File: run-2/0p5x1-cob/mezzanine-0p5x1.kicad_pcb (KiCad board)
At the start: 2 copper layers, 14 x 16 mm, 11 parts

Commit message: Layers, text
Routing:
- added copper zone on In1.Cu, net GND
- added copper zone on In2.Cu, net GND
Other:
- copper layers 2 -> 4
- board text added: "wafer.space GF180MCU Run 2"
- board text removed: "wafer.space GF180MCU Run 1"
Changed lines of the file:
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@@
 	(generator_version "10.0")
 	(general
-		(thickness 1.6)
+		(thickness 0.747)
 		(legacy_teardrops no)
 	)
@@
 	(layers
 		(0 "F.Cu" signal)
+		(4 "In1.Cu" signal)
+		(6 "In2.Cu" signal)
 		(2 "B.Cu" signal)
 		(9 "F.Adhes" user "F.Adhesive")
@@
 			(layer "F.Cu"
 				(type "copper")
-				(thickness 0.035)
+				(thickness 0.0175)
 			)
 			(layer "dielectric 1"
+				(type "prepreg")
+				(thickness 0.196)
+				(material "FR4")
+				(epsilon_r 4.5)
+				(loss_tangent 0.02)
+			)
+			(layer "In1.Cu"
+				(type "copper")
+				(thickness 0.035)
+			)
+			(layer "dielectric 2"
 				(type "core")
-				(thickness 1.51)
+				(thickness 0.23)
 				(material "FR4")
 				(epsilon_r 4.5)
 				(loss_tangent 0.02)
 			)
-			(layer "B.Cu"
+			(layer "In2.Cu"
 				(type "copper")
 				(thickness 0.035)
 			)
+			(layer "dielectric 3"
+				(type "prepreg")
+				(thickness 0.196)
+				(material "FR4")
+				(epsilon_r 4.5)
+				(loss_tangent 0.02)
+			)
+			(layer "B.Cu"
+				(type "copper")
+				(thickness 0.0175)
+			)
 			(layer "B.Mask"
 				(type "Bottom Solder Mask")
@@
 		)
 	)
-	(gr_text "wafer.space \nGF180MCU Run 1"
+	(gr_text "wafer.space \nGF180MCU Run 2"
 		(at 88.93 92.044999 270)
 		(layer "B.SilkS")
@@
 			(justify bottom mirror)
 		)
-		(render_cache "wafer.space \nGF180MCU Run 1" 270
+		(render_cache "wafer.space \nGF180MCU Run 2" 270
 			(polygon
 				(pts
@@
 			(polygon
 				(pts
-					(xy 89.1 86.624089) (xy 89.1 86.74444) (xy 89.798595 86.74444) (xy 89.895193 86.743097) (xy 89.970786 86.738883)
-					(xy 89.93299 86.779489) (xy 89.893789 86.825651) (xy 89.807021 86.932079) (xy 89.889576 86.996437)
-					(xy 90.099624 86.726244) (xy 90.099624 86.624089)
+					(xy 89.1 86.393035) (xy 89.1 87.053834) (xy 89.202215 87.053834) (xy 89.466791 86.792067) (xy 89.601186 86.664695)
+					(xy 89.661134 86.618037) (xy 89.716652 86.586293) (xy 89.775469 86.566441) (xy 89.840605 86.55967)
+					(xy 89.893507 86.565667) (xy 89.934318 86.582236) (xy 89.965901 86.608702) (xy 89.989091 86.64355)
+					(xy 90.003483 86.685388) (xy 90.008583 86.736075) (xy 90.001991 86.805936) (xy 89.983365 86.86418)
+					(xy 89.954109 86.918656) (xy 89.913389 86.976837) (xy 89.996004 87.04266) (xy 90.040859 86.980226)
+					(xy 90.079291 86.907594) (xy 90.098056 86.855691) (xy 90.109618 86.798796) (xy 90.113607 86.736075)
+					(xy 90.10865 86.666053) (xy 90.094704 86.607008) (xy 90.072697 86.557096) (xy 90.042899 86.514852)
+					(xy 90.004887 86.479837) (xy 89.960593 86.454729) (xy 89.908768 86.439132) (xy 89.847627 86.433641)
+					(xy 89.796086 86.437274) (xy 89.747256 86.448023) (xy 89.700593 86.465881) (xy 89.633788 86.50353)
+					(xy 89.565465 86.555457) (xy 89.498582 86.615972) (xy 89.423377 86.689852) (xy 89.217602 86.898435)
+					(xy 89.211985 86.898435) (xy 89.211985 86.393035)
 				)
 			)
@@
 	(zone
 		(net "GND")
-		(layers "F.Cu" "B.Cu")
+		(layers "F.Cu" "B.Cu" "In1.Cu" "In2.Cu")
 		(hatch edge 0.5)
 		(connect_pads

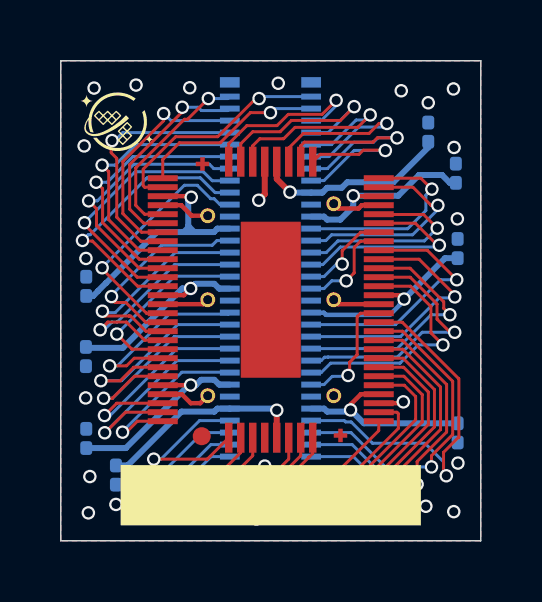
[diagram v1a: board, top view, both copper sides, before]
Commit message: Remove vias from centre of 0p5x1 and 1x1
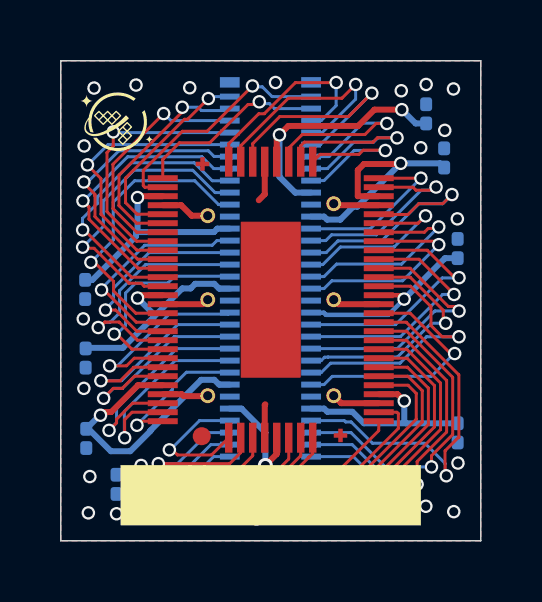
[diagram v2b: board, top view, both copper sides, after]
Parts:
- moved C103 0.64 mm to (92.5, 87.8)
- moved C101 0.61 mm to (91.9, 86.3)
- moved C102 0.31 mm to (81.6, 98.7)
- moved C108 0.11 mm to (80.6, 92.2), turned to -90 degrees
- moved C106 0.05 mm to (80.6, 94.5)
- turned C104 to -90 degrees
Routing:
- net /bidir_10: track 4.21 -> 8.30 mm
- net /bidir_17: track 3.13 -> 7.01 mm
- net /bidir_16: track 3.40 -> 6.91 mm
- net VDD_CORE_1: track 6.74 -> 9.31 mm
- net VDD_IO_1: track 6.63 -> 9.03 mm, vias 1 -> 2
- net VDD_IO_3: track 7.08 -> 9.04 mm, vias 1 -> 2
- net /bidir_33: track 8.28 -> 10.2 mm
- net VDD_CORE_0: track 6.66 -> 8.44 mm
- net GND: track 10.3 -> 11.9 mm, vias 24 -> 22
- net /bidir_19: track 6.68 -> 8.22 mm
- net /rst_n: track 7.47 -> 6.21 mm
- net /clk: track 5.86 -> 4.71 mm
- net /bidir_43: track 5.91 -> 4.82 mm
- net /in_0: track 7.20 -> 8.26 mm
- net /bidir_21: track 6.80 -> 5.77 mm
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
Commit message: Arrow marking, tweak ground flood on 1x1
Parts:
- added G***: LOGO, WaferSpace:ws_top_arrow, F.Cu at (90.6, 87.8)

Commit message: Matching pin 1 through hole on 1x1, 1x0p5, 0p5x1
Remove unneded via annualar rings from 1x0p5 and 0p5x1
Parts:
- added J1: Conn_01x01, WaferSpace:pin1_fiducial, F.Cu at (81.0, 99.4)
- moved C102 0.62 mm to (81.2, 98.2), turned to 180 degrees
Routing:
- net GND: track 11.9 -> 12.9 mm, vias 22 -> 19

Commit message: panelize half slots
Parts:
- moved J1 0.21 mm to (81.1, 99.2)
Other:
- board text added: "1"
